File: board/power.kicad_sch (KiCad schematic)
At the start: 27 parts

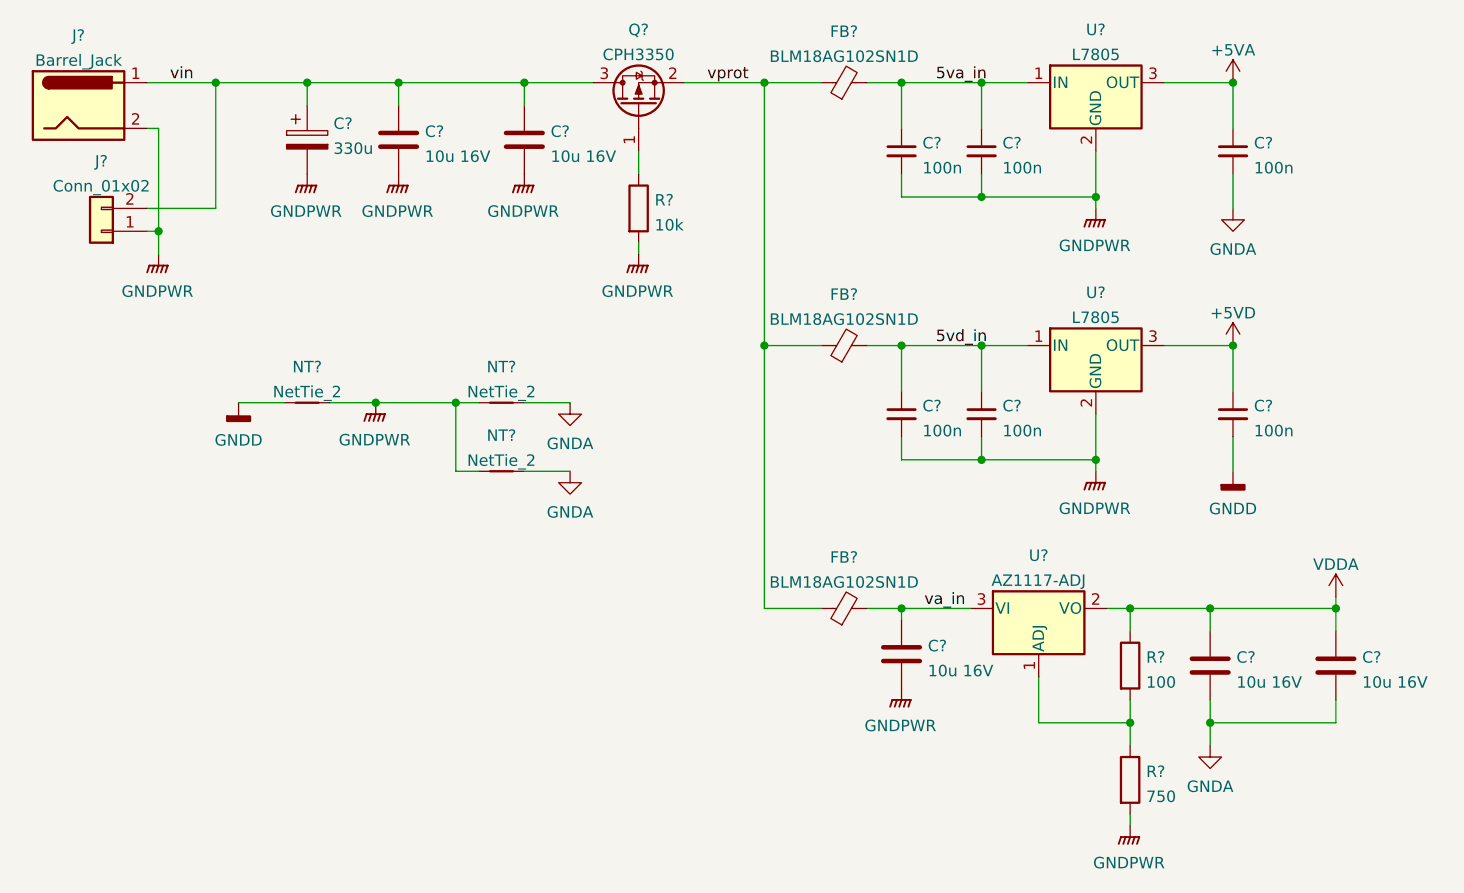
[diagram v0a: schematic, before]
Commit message: schema for test of dac done
start layout
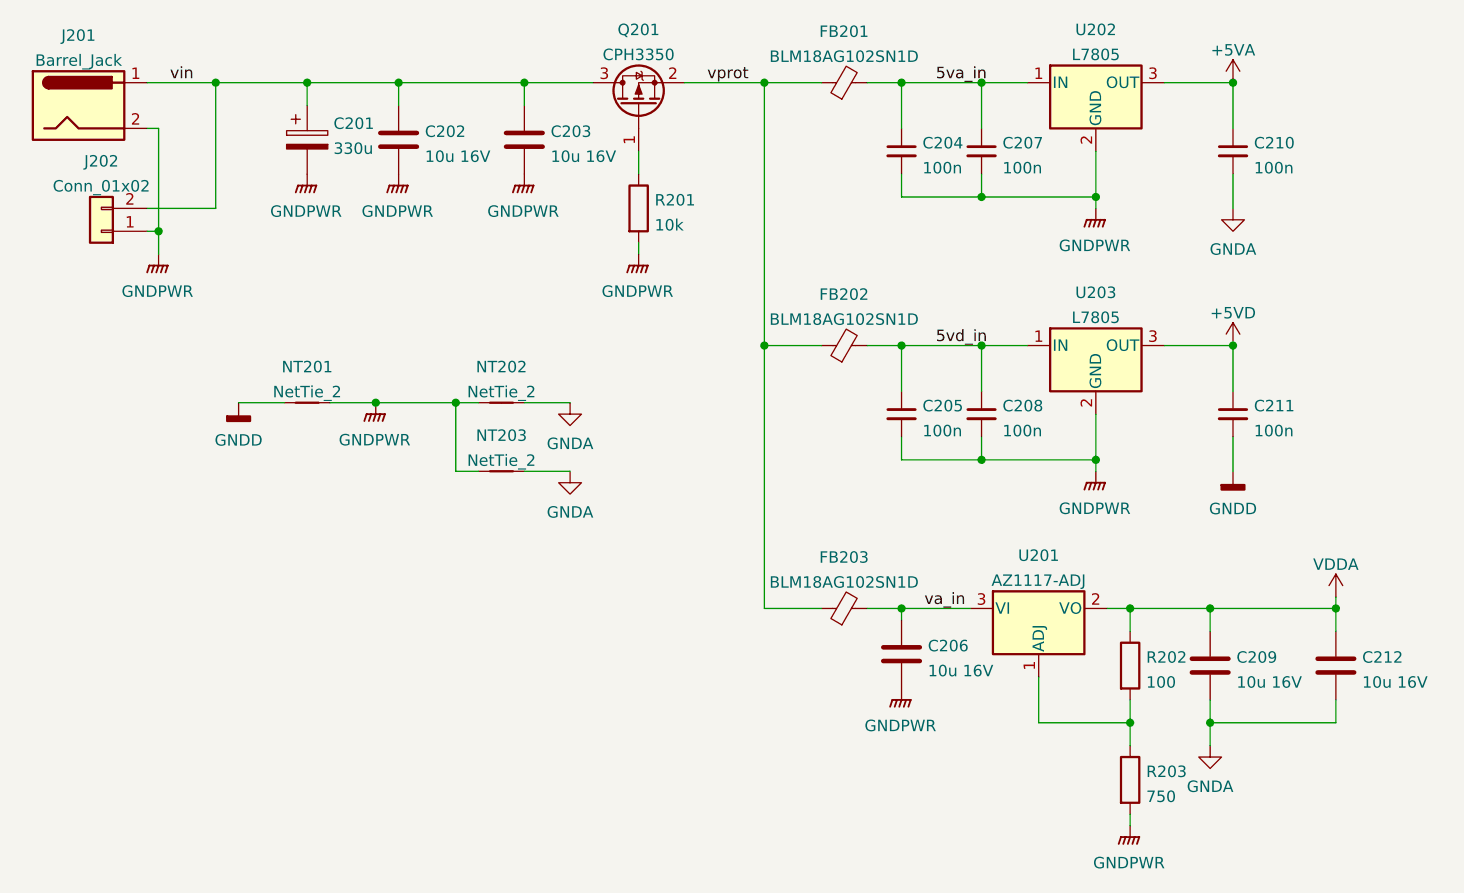
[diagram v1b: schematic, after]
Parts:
- NT201, NT202, NT203: renamed from NT?; footprint (none) -> NetTie:NetTie-2_SMD_Pad2.0mm
- Q201: renamed from Q?; footprint (none) -> Package_TO_SOT_SMD:SOT-23_Handsoldering
- U201: renamed from U?; footprint (none) -> Package_TO_SOT_SMD:TO-252-3_TabPin2
- U202, U203: renamed from U?; footprint (none) -> Package_TO_SOT_THT:TO-220-3_Vertical
- gave numbers to parts that had none: 20

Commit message: some pcb digital moved
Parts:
- C201: footprint (none) -> Capacitor_SMD:CP_Elec_10x10
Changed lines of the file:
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@@
       (effects (font (size 1.27 1.27)) (justify left))
     )
-    (property "Footprint" "" (id 2) (at 91.1352 62.23 0)
+    (property "Footprint" "Capacitor_SMD:CP_Elec_10x10" (id 2) (at 91.1352 62.23 0)
       (effects (font (size 1.27 1.27)) hide)
     )
